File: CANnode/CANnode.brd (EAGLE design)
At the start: 57.9 x 57.7 mm, 247 parts, among them IC1 ISO1050DUB, IC2 ISO1050DUB, Q1 FDV302P, Q3 FDV302P, U1 LM324PW, U10 FT2232HL, U11 93LC56C-I/SN, U2 TPS70445_PWP_24, U3 LM324PW, U4 LM324PW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

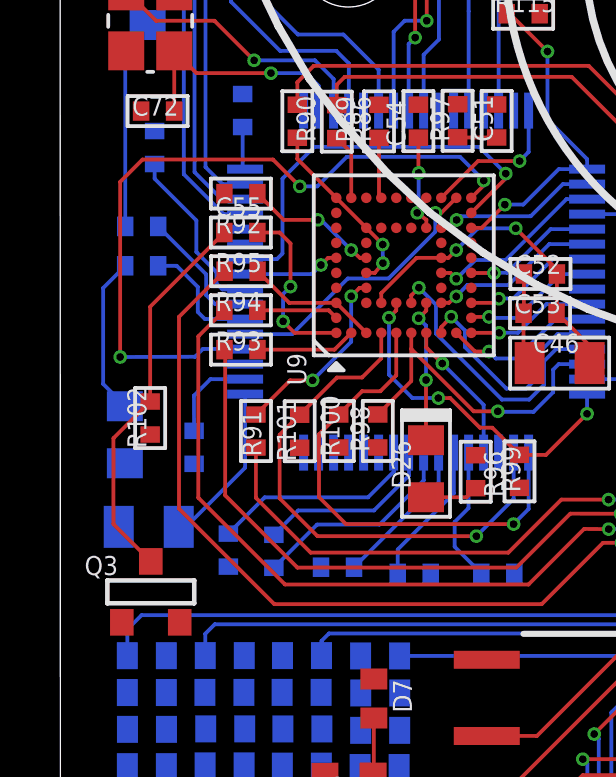
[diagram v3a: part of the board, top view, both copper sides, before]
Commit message: Started drawing power planes
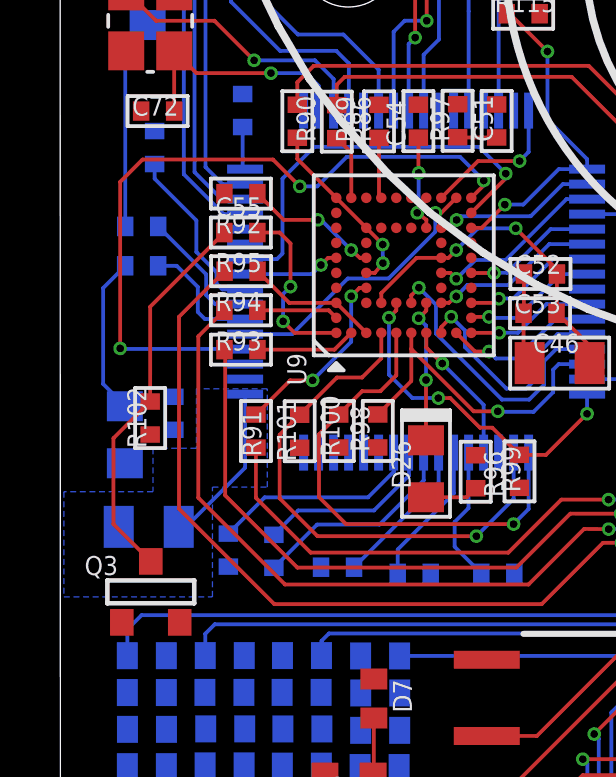
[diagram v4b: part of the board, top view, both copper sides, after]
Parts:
- moved C67 1.32 mm to (11.7, 36.3)
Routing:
- net +3V3: track 72.8 -> 69.7 mm
- added copper zone on layer 15, net +1V8
- added copper zone on layer 16, net +1V8
- added copper zone on layer 2, net GND
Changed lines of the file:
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@@
 <setting verticaltext="up"/>
 </settings>
-<grid distance="0.000123031496" unitdist="mil" unit="mil" style="lines" multiple="1" display="no" altdistance="0.025" altunitdist="inch" altunit="inch"/>
+<grid distance="3" unitdist="mil" unit="mil" style="lines" multiple="1" display="no" altdistance="0.025" altunitdist="inch" altunit="inch"/>
 <layers>
 <layer number="1" name="Top" color="12" fill="1" visible="no" active="yes"/>
-<layer number="2" name="Route2" color="6" fill="1" visible="yes" active="yes"/>
-<layer number="15" name="Route15" color="4" fill="6" visible="no" active="yes"/>
+<layer number="2" name="Route2" color="2" fill="1" visible="no" active="yes"/>
+<layer number="15" name="Route15" color="6" fill="1" visible="yes" active="yes"/>
 <layer number="16" name="Bottom" color="1" fill="1" visible="yes" active="yes"/>
 <layer number="17" name="Pads" color="2" fill="1" visible="no" active="yes"/>
@@
 <attribute name="NAME" x="27.505446875" y="43.07509375" size="0.635" layer="26" rot="MR270"/>
 </element>
-<element name="C67" library="launchpad" package="0402" value="100nF" x="12.41828125" y="35.15926875" smashed="yes" rot="MR270">
-<attribute name="NAME" x="12.44528125" y="35.70346875" size="0.635" layer="26" rot="MR270"/>
+<element name="C67" library="launchpad" package="0402" value="100nF" x="11.743665625" y="36.29471875" smashed="yes" rot="MR270">
+<attribute name="NAME" x="11.770665625" y="36.83891875" size="0.635" layer="26" rot="MR270"/>
 </element>
 <element name="C68" library="launchpad" package="0402" value="100nF" x="27.764934375" y="61.9141875" smashed="yes" rot="MR90">
@@
 <wire x1="25.520003125" y1="37.43249375" x2="25.51925" y2="37.433246875" width="0.127" layer="16"/>
 <wire x1="14.118759375" y1="37.4337375" x2="14.11925" y2="37.433246875" width="0.127" layer="16"/>
-<wire x1="12.4139125" y1="36.882246875" x2="12.962984375" y2="37.43131875" width="0.127" layer="16"/>
-<wire x1="12.962984375" y1="37.43131875" x2="14.117321875" y2="37.43131875" width="0.127" layer="16"/>
 <wire x1="14.117321875" y1="37.43131875" x2="14.11925" y2="37.433246875" width="0.127" layer="16"/>
-<wire x1="12.4139125" y1="36.882246875" x2="12.41828125" y2="35.70926875" width="0.127" layer="16"/>
 <wire x1="35.63740625" y1="29.932634375" x2="34.618753125" y2="29.932634375" width="0.127" layer="1"/>
 <wire x1="34.618753125" y1="29.932634375" x2="33.629896875" y2="30.921490625" width="0.127" layer="1"/>
@@
 <wire x1="12.49533125" y1="42.721253125" x2="14.52895625" y2="43.616875" width="0" layer="19" extent="1-16"/>
 <wire x1="14.11925" y1="37.433246875" x2="14.108565625" y2="40.4225625" width="0" layer="19" extent="16-16"/>
-<wire x1="10.110765625" y1="34.627253125" x2="12.41828125" y2="35.70926875" width="0" layer="19" extent="16-16"/>
+<wire x1="11.743665625" y1="36.84471875" x2="14.11925" y2="37.433246875" width="0" layer="19" extent="16-16"/>
+<wire x1="10.110765625" y1="34.627253125" x2="11.743665625" y2="36.84471875" width="0" layer="19" extent="16-16"/>
 <wire x1="15.93839375" y1="35.14673125" x2="14.11925" y2="37.433246875" width="0" layer="19" extent="1-16"/>
 <wire x1="17.2411" y1="35.15308125" x2="15.93839375" y2="35.14673125" width="0" layer="19" extent="1-1"/>
@@
 <vertex x="31.6992" y="59.8932"/>
 </polygon>
+<polygon width="0.127" layer="2">
+<vertex x="8.0772" y="70.1802"/>
+<vertex x="65.8368" y="70.1802"/>
+<vertex x="65.8368" y="12.4206"/>
+<vertex x="8.001" y="12.4206"/>
+<vertex x="8.001" y="70.1802"/>
+</polygon>
 <wire x1="47.819321875" y1="63.37565625" x2="47.908528125" y2="66.45870625" width="0" layer="19" extent="16-16"/>
 <wire x1="45.80615" y1="61.41909375" x2="47.819321875" y2="63.37565625" width="0" layer="19" extent="1-16"/>
@@
 <wire x1="10.197434375" y1="25.75806875" x2="12.805575" y2="25.77630625" width="0" layer="19" extent="16-16"/>
 <wire x1="13.561475" y1="31.182840625" x2="14.091859375" y2="28.21799375" width="0" layer="19" extent="16-16"/>
-<wire x1="12.41828125" y1="34.60926875" x2="13.561475" y2="31.182840625" width="0" layer="19" extent="16-16"/>
-<wire x1="10.95371875" y1="35.585784375" x2="12.41828125" y2="34.60926875" width="0" layer="19" extent="1-16"/>
-<wire x1="9.906090625" y1="32.5086375" x2="10.95371875" y2="35.585784375" width="0" layer="19" extent="1-16"/>
-<wire x1="14.11925" y1="37.933246875" x2="12.41828125" y2="34.60926875" width="0" layer="19" extent="16-16"/>
+<wire x1="9.906090625" y1="32.5086375" x2="13.561475" y2="31.182840625" width="0" layer="19" extent="16-16"/>
+<wire x1="10.95371875" y1="35.585784375" x2="9.906090625" y2="32.5086375" width="0" layer="19" extent="1-16"/>
+<wire x1="11.743665625" y1="35.74471875" x2="10.95371875" y2="35.585784375" width="0" layer="19" extent="1-16"/>
+<wire x1="14.11925" y1="37.933246875" x2="11.743665625" y2="35.74471875" width="0" layer="19" extent="16-16"/>
 <wire x1="16.56925" y1="34.983246875" x2="14.11925" y2="37.933246875" width="0" layer="19" extent="16-16"/>
 <wire x1="14.054975" y1="56.29995" x2="14.754978125" y2="51.827340625" width="0" layer="19" extent="16-16"/>
@@
 <contactref element="U9" pad="K10"/>
 <contactref element="U10" pad="52"/>
-<via x="9.953340625" y="38.16989375" extent="1-16" drill="0.254"/>
+<via x="9.953340625" y="38.455934375" extent="1-16" drill="0.254"/>
 <via x="15.941634375" y="43.85754375" extent="1-16" drill="0.254"/>
 <wire x1="15.941634375" y1="43.85754375" x2="16.523253125" y2="43.85754375" width="0.127" layer="16"/>
@@
 <wire x1="22.071884375" y1="43.88935" x2="21.657403125" y2="43.47486875" width="0.127" layer="1"/>
 <wire x1="15.046740625" y1="44.7524375" x2="15.941634375" y2="43.85754375" width="0.127" layer="1"/>
-<wire x1="9.953340625" y1="38.16989375" x2="12.450525" y2="38.178221875" width="0.127" layer="16"/>
-<wire x1="12.450525" y1="38.178221875" x2="12.711609375" y2="38.43930625" width="0.127" layer="16"/>
-<wire x1="12.711609375" y1="38.43930625" x2="14.113190625" y2="38.43930625" width="0.127" layer="16"/>
 <wire x1="14.113190625" y1="38.43930625" x2="14.11925" y2="38.433246875" width="0.127" layer="16"/>
 <wire x1="15.046740625" y1="44.7524375" x2="10.698859375" y2="44.7524375" width="0.127" layer="1"/>
 <wire x1="10.698859375" y1="44.7524375" x2="9.953340625" y2="44.00691875" width="0.127" layer="1"/>
-<wire x1="9.953340625" y1="44.00691875" x2="9.953340625" y2="38.16989375" width="0.127" layer="1"/>
+<wire x1="9.953340625" y1="44.00691875" x2="9.953340625" y2="38.455934375" width="0.127" layer="1"/>
+<wire x1="14.113190625" y1="38.43930625" x2="9.953340625" y2="38.43930625" width="0.127" layer="16"/>
+<wire x1="9.953340625" y1="38.43930625" x2="9.953340625" y2="38.455934375" width="0.127" layer="16"/>
 </signal>
 <signal name="CPLD_TDI">
@@
 <wire x1="21.10311875" y1="31.846996875" x2="21.98878125" y2="30.961334375" width="0.127" layer="16"/>
 <wire x1="21.98878125" y1="30.961334375" x2="21.991621875" y2="30.961334375" width="0.127" layer="16"/>
+<polygon width="0.127" layer="16">
+<vertex x="14.859" y="37.1094"/>
+<vertex x="12.4968" y="37.1094"/>
+<vertex x="12.4968" y="35.1282"/>
+<vertex x="11.049" y="35.1282"/>
+<vertex x="11.049" y="33.6804"/>
+<vertex x="8.0772" y="33.6804"/>
+<vertex x="8.0772" y="30.1752"/>
+<vertex x="13.0302" y="30.1752"/>
+<vertex x="13.0302" y="33.8328"/>
+<vertex x="14.859" y="33.8328"/>
+</polygon>
+<polygon width="0.127" layer="15">
+<vertex x="22.3266" y="52.959"/>
+<vertex x="12.954" y="52.959"/>
+<vertex x="12.954" y="44.196"/>
+<vertex x="15.621" y="44.196"/>
+<vertex x="15.621" y="37.0332"/>
+<vertex x="11.2776" y="37.0332"/>
+<vertex x="11.2776" y="33.6042"/>
+<vertex x="8.3058" y="33.6042"/>
+<vertex x="8.3058" y="30.0228"/>
+<vertex x="13.1826" y="30.0228"/>
+<vertex x="13.1826" y="33.6804"/>
+<vertex x="17.907" y="33.6804"/>
+<vertex x="17.907" y="36.0426"/>
+<vertex x="21.4122" y="36.0426"/>
+<vertex x="21.4122" y="29.8704"/>
+<vertex x="26.4414" y="29.8704"/>
+<vertex x="26.4414" y="31.5468"/>
+<vertex x="22.6314" y="31.5468"/>
+<vertex x="22.6314" y="52.959"/>
+</polygon>
 <wire x1="19.895409375" y1="45.482021875" x2="21.56925" y2="46.383246875" width="0" layer="19" extent="1-16"/>
 <wire x1="14.11925" y1="44.433246875" x2="19.895409375" y2="44.316696875" width="0" layer="19" extent="1-16"/>

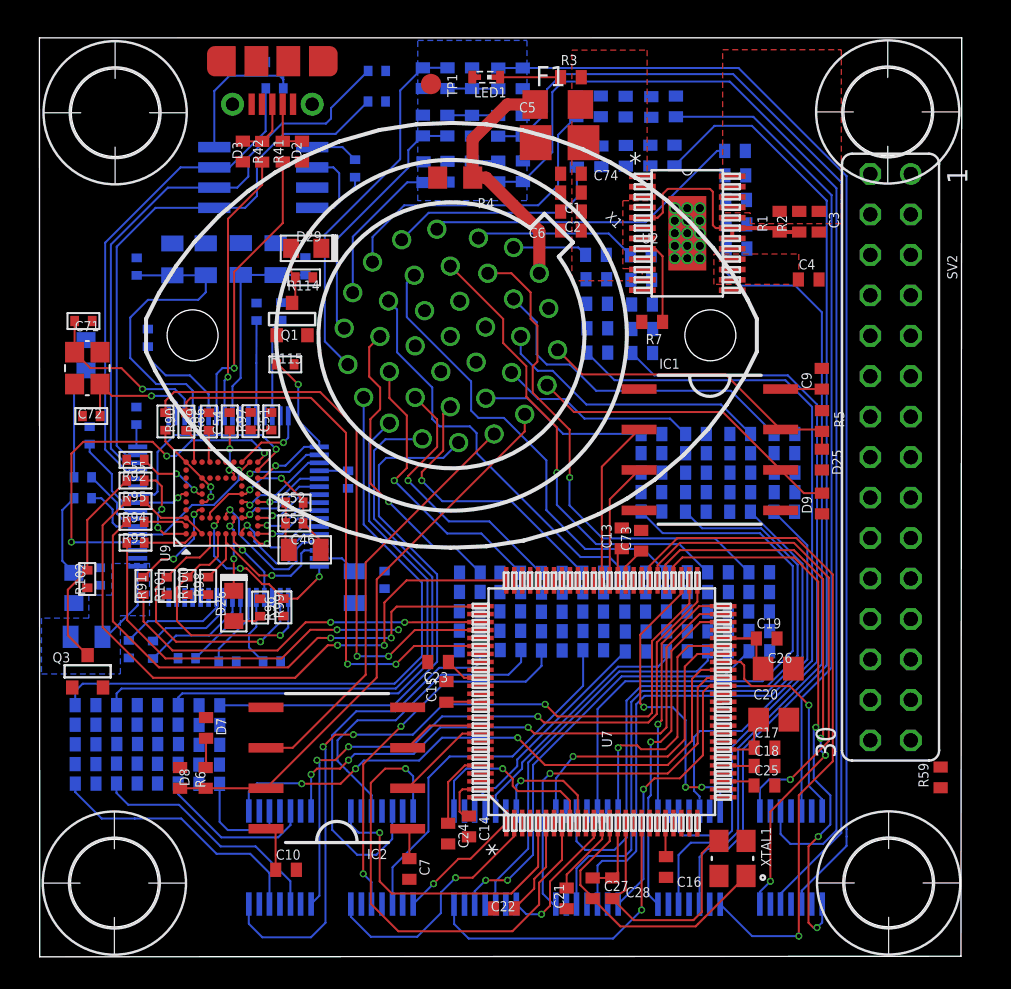
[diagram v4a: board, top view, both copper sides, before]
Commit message: Continued working on power planes
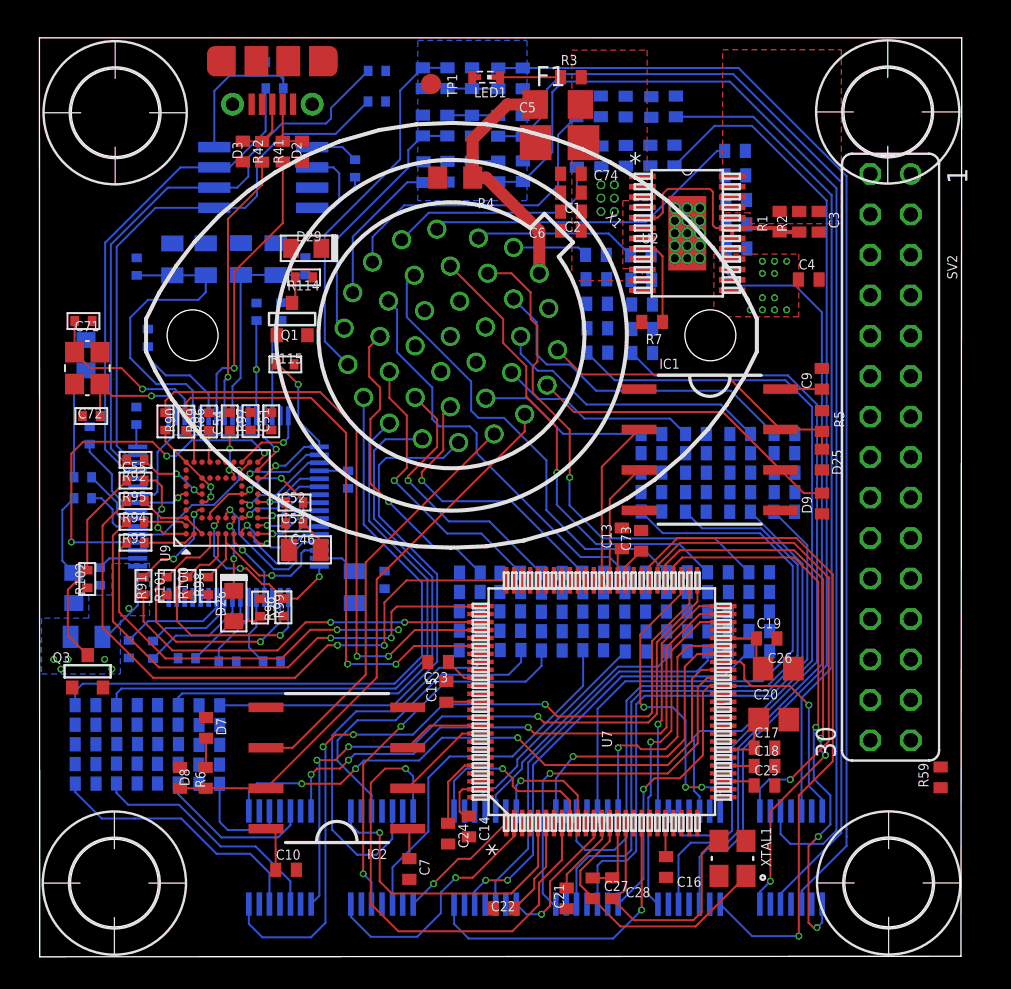
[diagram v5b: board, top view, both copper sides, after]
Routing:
- net +3V3: track 69.7 -> 72.3 mm
- net +1V8: vias 2 -> 9
- net +5V: vias 0 -> 6
- net +1V2: vias 0 -> 11
- added copper zone on layer 15, net +3V3
- added copper zone on layer 15, net +5V
- added copper zone on layer 15, net N$10

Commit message: Routed +5V, +1V8, +1V2
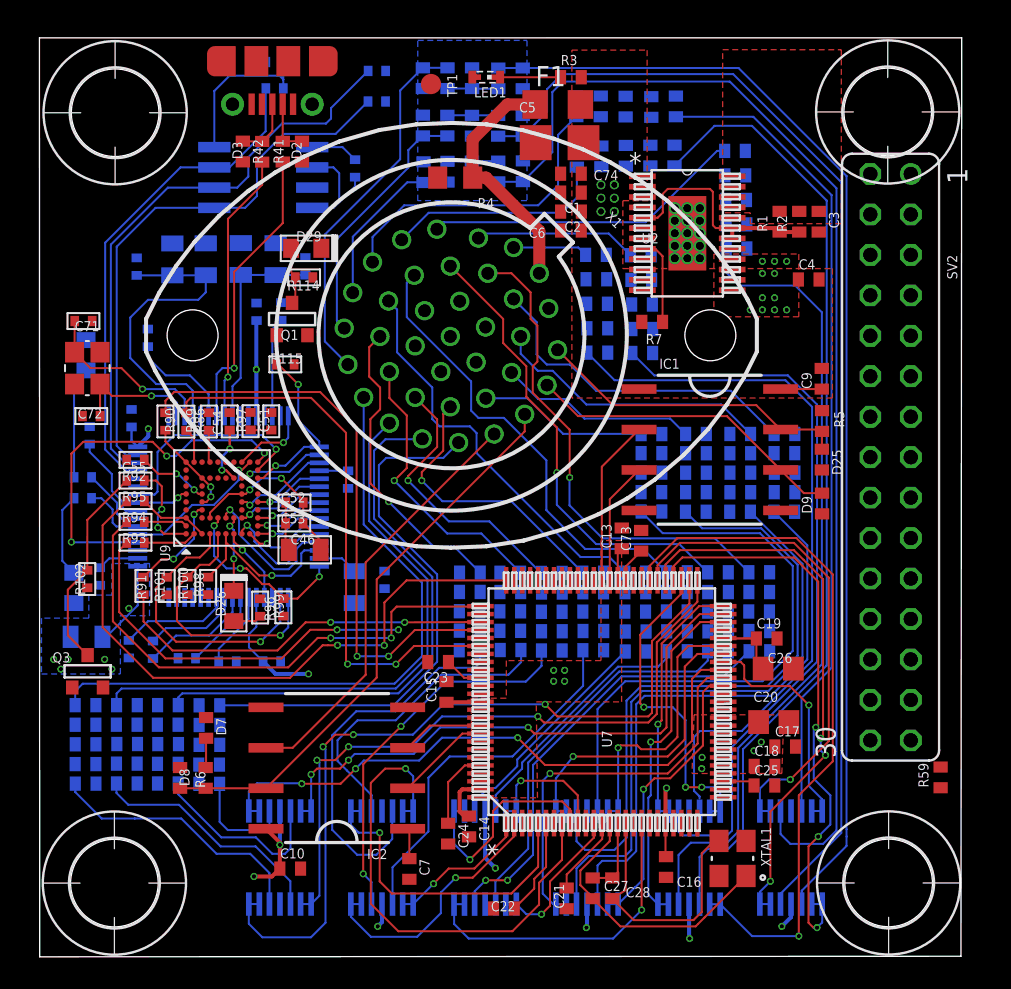
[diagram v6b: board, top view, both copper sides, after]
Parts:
- moved C17 1.30 mm to (54.8, 25.6)
- moved C62 0.34 mm to (13.7, 46.2)
- moved C10 0.27 mm to (23.7, 18.0)
- moved C20 0.15 mm to (54.1, 27.2)
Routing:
- net +5V: track 5.77 -> 20.3 mm, vias 6 -> 13
- net +1V8: track 20.7 -> 25.8 mm, vias 9 -> 11
- net +1V2: track 15.1 -> 12.3 mm, vias 11 -> 20
- net D4_BUFFERED: track 12.0 -> 13.9 mm
- net A1_3V3: track 10.1 -> 11.8 mm
- net D0_BUFFERED: track 7.95 -> 9.11 mm
- net D7_BUFFERED: track 19.6 -> 20.3 mm
- net D2_BUFFERED: track 19.6 -> 20.3 mm
- net D1_BUFFERED: track 15.8 -> 16.4 mm
- net A9_BUFFERED: track 21.1 -> 21.8 mm
- net A7_BUFFERED: track 14.0 -> 14.7 mm
- net A4_BUFFERED: track 35.6 -> 36.3 mm
- net A3_BUFFERED: track 49.4 -> 50.0 mm
- net A15_BUFFERED: track 16.4 -> 17.0 mm
- net A0_BUFFERED: track 37.9 -> 38.5 mm
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- added copper zone on layer 15, net +1V2
- removed copper zone on layer 15, net N$10

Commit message: Started grounding input stages
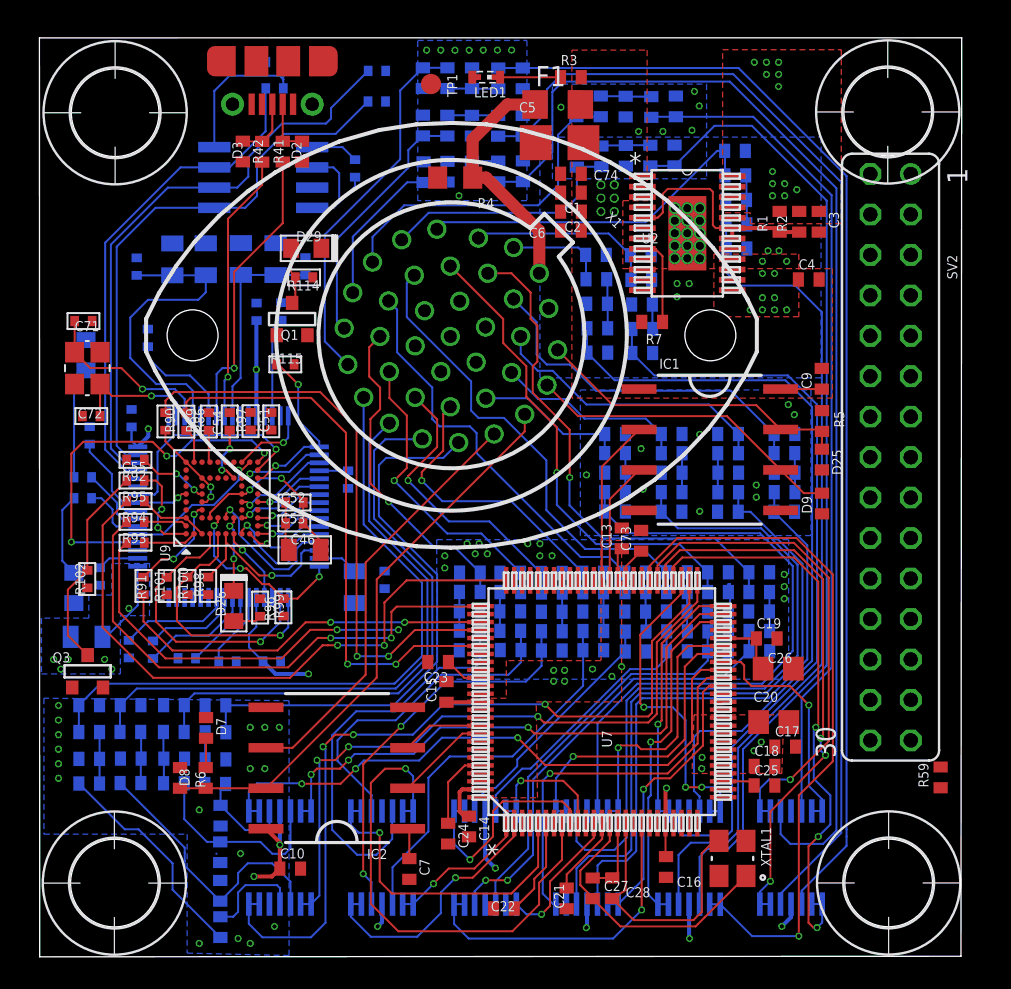
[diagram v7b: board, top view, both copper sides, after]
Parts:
- moved R15 12.4 mm to (19.3, 14.3), turned to 270 degrees
- moved R13 8.93 mm to (19.3, 16.6), turned to 270 degrees
- moved R11 5.42 mm to (19.3, 19.0), turned to 90 degrees
- moved C47 2.29 mm to (44.1, 42.8)
- moved D31 2.29 mm to (44.1, 45.2)
- moved R38 2.29 mm to (44.1, 41.6)
- moved R39 2.29 mm to (44.1, 40.4)
- moved R81 2.29 mm to (44.1, 44.0)
- moved R9 2.12 mm to (19.3, 21.3), turned to 90 degrees
- moved C42 1.52 mm to (47.6, 42.8)
- moved D18 1.52 mm to (47.6, 45.2)
- moved R36 1.52 mm to (47.6, 41.6)
- moved R37 1.52 mm to (47.6, 40.4)
- moved R76 1.52 mm to (47.6, 44.0)
- moved R10 1.28 mm to (16.4, 23.3)
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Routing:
- net GND: track 6.08 -> 12.4 mm, vias 0 -> 61
- net N$62: track 0.00 -> 3.69 mm
- net N$46: track 0.00 -> 3.26 mm
- net N$45: track 0.00 -> 3.26 mm
- net N$68: track 0.00 -> 3.24 mm
- net N$57: track 0.00 -> 3.24 mm
- net N$67: track 0.00 -> 3.19 mm
- net N$59: track 0.00 -> 3.11 mm
- net N$55: track 0.00 -> 3.10 mm
- net N$66: track 0.00 -> 3.10 mm
- net N$48: track 0.00 -> 3.09 mm
- net A15_3V3: track 36.4 -> 39.5 mm
- net A3_3V3: track 16.8 -> 13.9 mm
- net A14_3V3: track 40.2 -> 43.0 mm
- net N$51: track 0.00 -> 2.51 mm
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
